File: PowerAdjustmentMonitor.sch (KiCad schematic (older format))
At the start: 37 parts, among them U5 LM317K, U6 LM337T, U7 LM337T, U8 LM317

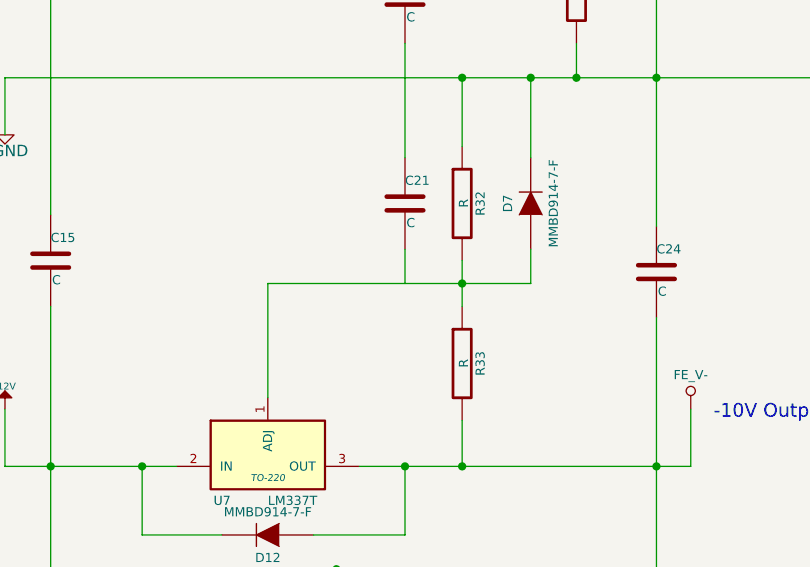
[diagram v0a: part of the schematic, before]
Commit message: Cleanup/ERC checks, etc (on my own, no video)
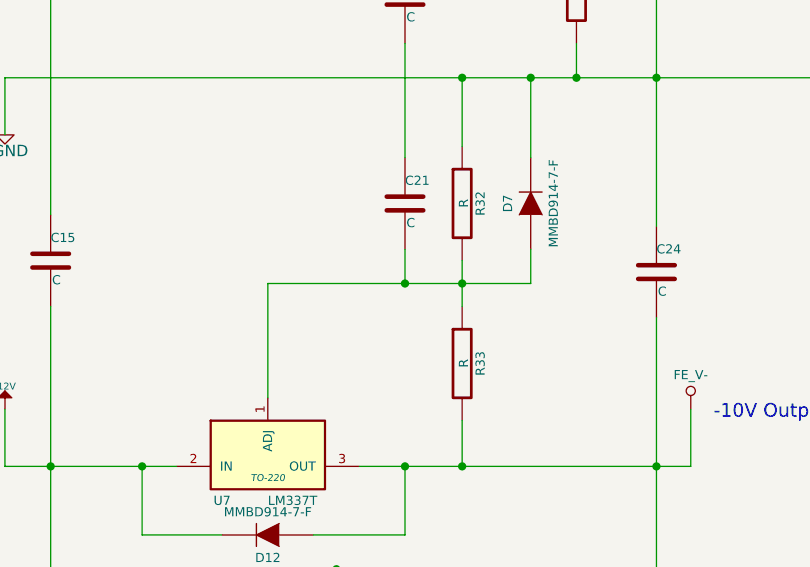
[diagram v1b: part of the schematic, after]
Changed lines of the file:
@@
 Connection ~ 5150 5600
 Connection ~ 5150 7550
+Connection ~ 4050 4800
 $EndSCHEMATC
